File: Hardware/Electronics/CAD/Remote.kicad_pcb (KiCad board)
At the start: 2 copper layers, 191 x 32 mm, 48 parts, among them J1 CONN_01X12, J2 CONN_01X03, J3 CONN_01X05, J4 CONN_01X01, J5 CONN_01X01, J6 CONN_01X24, Q1 AO3418, Q2 Q_NPN_BCE, SW1 SW_DPST_x2, U2 MCP23S17, U3 ESP-12E, U4 LD1117S33CTR

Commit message: update design
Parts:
- removed Q2: Q_NPN_BCE, TO_SOT_Packages_SMD:SOT-23
- removed R14: 10K, Resistors_SMD:R_0805
- removed R15: 1K, Resistors_SMD:R_0805
- removed REF**: ePaper_1.54in, ePaper:ePaper_1.54in
- removed SW1: SW_DPST_x2, Buttons_Switches_SMD:SW_SPST_SKQG
- removed U4: LD1117S33CTR, TO_SOT_Packages_SMD:SOT-223
- added C15: 4,7uF, Capacitors_SMD:C_0805, B.Cu at (167.6, 64.0)
- added C16: 4,7uF, Capacitors_SMD:C_0805, B.Cu at (169.7, 64.0)
- added C17: 4,7uF, Capacitors_SMD:C_0805, B.Cu at (159.5, 68.1)
- added U1: ATMEGA328P-AU, Housings_QFP:TQFP-32_7x7mm_Pitch0.8mm, B.Cu at (159.8, 48.0)
- added Y1: Resonator, Crystals:Resonator_SMD-3pin_7.2x3.0mm, B.Cu at (145.3, 37.3)
- C1: value CP_Small -> 100nF; footprint Capacitor:CP_8x11.5mm_hor -> Capacitors_SMD:C_0805; moved to B.Cu
- C10, C11, C12, C13, C14, C6, C7, C8, C9: value 1uF -> 4,7uF; moved to B.Cu
- C2: value CP_Small -> 1uF; footprint Capacitor:CP_8x11.5mm_hor -> Capacitors_SMD:C_0805; moved to B.Cu
- C3: value 4.7uF -> 1uF; moved to B.Cu
- C4: value 1uF -> 22nF; moved to B.Cu
- C5: value 1uF -> 100nF; moved to B.Cu
- D2: value MBR0520 -> SFH203FA; footprint Diodes_SMD:D_SOD-123 -> LED_castellation:LED_D3.0mm_Horizontal_O6.35mm_Z2.0mm
- D3, D4: value MBR0520 -> MBR0530; moved to B.Cu
- D5: value SFH203FA -> MBR0530; footprint LED_castellation:LED_D3.0mm_Horizontal_O6.35mm_Z2.0mm -> Diodes_SMD:D_SOD-123; moved to B.Cu
- J1: value CONN_01X12 -> CONN_01X01; footprint Terminal:SolderPad_1x12_1.27mm -> SMD_Packages:1Pin
- J2: value CONN_01X03 -> CONN_01X01; footprint Terminal:Pin_Header_SMD_1x3_Angled_2.54mm -> SMD_Packages:1Pin; moved to B.Cu
- J3: value CONN_01X05 -> CONN_02X03; footprint Terminal:SolderPad_1x5_3.81mm -> Pin_Headers:Pin_Header_Straight_2x03_Pitch2.54mm
- J4: value CONN_01X01 -> CONN_01X06; footprint SMD_Packages:1Pin -> Pin_Headers:Pin_Header_Straight_1x06_Pitch2.54mm
- J5: value CONN_01X01 -> CONN_01X12; footprint SMD_Packages:1Pin -> Terminal:SolderPad_1x12_1.27mm
- J6: moved to F.Cu
- L1: footprint Inductors_SMD:L_0805 -> Inductors_SMD:L_1806; moved to B.Cu
- Q1: value AO3418 -> SI1308EDL; footprint TO_SOT_Packages_SMD:SOT-23 -> TO_SOT_Packages_SMD:SOT-323_SC-70; moved to B.Cu
- R1: value 330 -> 10K; moved to B.Cu
- R10, R3: moved to B.Cu
- R11: value 10K -> 1K; moved to B.Cu
- R12: value 10K -> 3; moved to B.Cu
- R13, R4, R5, R7, R8, R9: value 10K -> 4,7K; moved to B.Cu
- R2: value RND 0805 1 10K -> 330; moved to B.Cu
- R6: value 3 -> 4,7K; moved to B.Cu
- U2: value MCP23S17 -> RT9193; footprint Housings_SOIC:SOIC-28W_7.5x17.9mm_Pitch1.27mm -> TO_SOT_Packages_SMD:SOT-23-5; moved to B.Cu
- U3: value ESP-12E -> MCP23S17; footprint ESP8266:ESP-12E_SMD -> SMD_Packages:SOIC-28; moved to B.Cu
- moved C1 95.6 mm to (167.6, 47.5)
- moved D2 76.9 mm to (212.6, 59.7), turned to 90 degrees
- moved R11 76.1 mm to (165.6, 68.1), turned to 270 degrees
- moved R13 67.5 mm to (152.1, 50.8), turned to 0 degrees
- moved D5 61.0 mm to (151.9, 65.5)
- moved R12 54.9 mm to (151.1, 57.9), turned to 0 degrees
- moved R10 54.4 mm to (151.1, 59.9), turned to 180 degrees
- moved R2 53.8 mm to (152.1, 49.0), turned to 180 degrees
- moved R7 48.9 mm to (134.6, 55.4), turned to 270 degrees
- moved R8 42.1 mm to (132.6, 55.4), turned to 270 degrees
- moved J4 38.7 mm to (78.7, 55.6), turned to 90 degrees
- moved R9 37.7 mm to (130.6, 55.4), turned to 270 degrees
- moved R1 36.2 mm to (167.4, 45.7), turned to 0 degrees
- moved R3 27.8 mm to (159.3, 55.4), turned to 90 degrees
- moved C5 27.5 mm to (161.0, 55.4), turned to 270 degrees
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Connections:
- C1 pad 1: Net-(C1-Pad1) -> Earth
- C1 pad 2: GND -> Net-(C1-Pad2)
- C10 pad 1: GND -> Earth
- C10 pad 2: VDD -> +3V3
- C11 pad 1: GND -> Earth
- C11 pad 2: VSH -> Net-(C11-Pad2)
- C12 pad 1: GND -> Earth
- C12 pad 2: VSL -> Net-(C12-Pad2)
- C13 pad 1: GND -> Earth
- C13 pad 2: VCOM -> Net-(C13-Pad2)
- C14 pad 1: GND -> Earth
- C14 pad 2: VPP -> PREVGH
- C2 pad 1: VCI -> Earth
- C2 pad 2: GND -> VCC
- C3 pad 1: GND -> Earth
- C3 pad 2: VCI -> +3V3
- C4 pad 1: Net-(C4-Pad1) -> Earth
- C5 pad 1: PREVGH -> ISP_CS
- C5 pad 2: GND -> UART_DTR
- C6 pad 1: PREVGL -> +3V3
- C6 pad 2: GND -> Earth
- C7 pad 1: GND -> Net-(C7-Pad1)
- C7 pad 2: VGL -> Net-(C7-Pad2)
- C8 pad 1: GND -> Earth
- C8 pad 2: VGH -> Net-(C8-Pad2)
- C9 pad 1: GND -> Earth
- C9 pad 2: VCI -> Net-(C9-Pad2)
- D1 pad 1: GND -> Earth
- D2 pad 1: PREVGH -> IR_LED_IN
- D2 pad 2: Net-(C4-Pad2) -> Net-(D2-Pad2)
- D3 pad 1: Net-(C4-Pad1) -> Earth
- D3 pad 2: PREVGL -> Net-(C7-Pad2)
- D4 pad 1: GND -> Net-(C7-Pad2)
- D4 pad 2: Net-(C4-Pad1) -> PREVGL
- D5 pad 1: Net-(D5-Pad1) -> PREVGH
- D5 pad 2: GND -> Net-(C7-Pad1)
- J1 pad 1: Net-(J1-Pad1) -> VCC
- J2 pad 1: VCI -> Earth
- J3 pad 1: TX -> SPI_MISO
- J3 pad 2: RX -> +3V3
- J3 pad 3: VCI -> SPI_CLK
- J3 pad 4: Net-(J3-Pad4) -> SPI_MOSI
- J3 pad 5: GND -> ISP_CS
- J4 pad 1: Net-(C1-Pad1) -> UART_DTR
- J5 pad 1: GND -> BTN5_IN
- J6 pad 1: Net-(J6-Pad1) -> (no net)
- J6 pad 10: RES# -> RST
- J6 pad 12: CS -> SPI_CS_DISP
- J6 pad 13: CLK -> SPI_CLK
- J6 pad 14: DIN -> SPI_MOSI
- J6 pad 15: VCI -> +3V3
- J6 pad 16: VCI -> +3V3
- J6 pad 17: GND -> Earth
- J6 pad 18: VDD -> Net-(C11-Pad2)
- J6 pad 19: VPP -> Net-(C12-Pad2)
- J6 pad 20: VSH -> Net-(C13-Pad2)
- J6 pad 22: VSL -> Net-(C15-Pad2)
- J6 pad 24: VCOM -> Net-(C17-Pad2)
- J6 pad 4: VGL -> Net-(C8-Pad2)
- J6 pad 5: VGH -> Net-(C9-Pad2)
- J6 pad 6: Net-(J6-Pad6) -> (no net)
- J6 pad 7: Net-(J6-Pad7) -> (no net)
- J6 pad 8: GND -> Net-(J6-Pad8)
- L1 pad 1: Net-(C4-Pad2) -> +3V3
- L1 pad 2: VCI -> Net-(C7-Pad1)
- Q1 pad 3: Net-(C4-Pad2) -> Net-(C7-Pad1)
- R1 pad 1: Net-(R1-Pad1) -> +3V3
- R1 pad 2: Net-(D1-Pad2) -> Net-(D2-Pad2)
- R10 pad 1: GND -> GDR
- R10 pad 2: Net-(J1-Pad8) -> Earth
- R11 pad 1: GND -> Net-(J6-Pad8)
- R11 pad 2: Net-(J1-Pad2) -> Earth
- R12 pad 1: GND -> Earth
- R12 pad 2: Net-(J1-Pad7) -> RESE
- R13 pad 1: VCI -> Earth
- R13 pad 2: Net-(D5-Pad1) -> IR_LED_IN
- R2 pad 1: GND -> IR_LED_OUT
- R2 pad 2: RESET -> Net-(D1-Pad2)
- R3 pad 1: GND -> +3V3
- R3 pad 2: CS -> ISP_CS
- R4 pad 1: VCI -> BTN0_IN
- R4 pad 2: RES# -> Earth
- R5 pad 1: GDR -> BTN1_IN
- R5 pad 2: GND -> Earth
- R6 pad 1: RESE -> BTN2_IN
- R6 pad 2: GND -> Earth
- R7 pad 1: GND -> BTN3_IN
- R7 pad 2: Net-(J1-Pad1) -> Earth
- R8 pad 1: GND -> BTN4_IN
- R8 pad 2: Net-(J1-Pad3) -> Earth
- R9 pad 1: GND -> BTN5_IN
- R9 pad 2: Net-(J1-Pad6) -> Earth
- U2 pad 1: Net-(J1-Pad5) -> VCC
- U2 pad 2: Net-(J1-Pad10) -> Earth
- U2 pad 3: Net-(J1-Pad12) -> VCC
- U2 pad 4: Net-(J1-Pad4) -> Net-(C4-Pad2)
- U2 pad 5: Net-(J1-Pad9) -> +3V3
- U3 pad 1: Net-(U3-Pad1) -> BTN0_IN
- U3 pad 10: CS -> Earth
- U3 pad 11: RES# -> SPI_CS_GPIO_EXP
- U3 pad 12: D/C -> SPI_CLK
- U3 pad 13: BUSY -> SPI_MOSI
- U3 pad 14: RESET -> SPI_MISO
- U3 pad 15: RX -> (no net)
- U3 pad 16: TX -> (no net)
- U3 pad 17: Net-(U2-Pad11) -> (no net)
- U3 pad 18: Net-(U2-Pad14) -> Earth
- U3 pad 19: Net-(U3-Pad19) -> GPIO_EXP_INT
- U3 pad 2: Net-(U3-Pad2) -> BTN1_IN
- U3 pad 20: Net-(U3-Pad20) -> (no net)
- U3 pad 21: Net-(U2-Pad13) -> BTN0_OUT
- U3 pad 22: Net-(U2-Pad12) -> BTN1_OUT
- U3 pad 3: VCI -> BTN2_IN
- U3 pad 4: Net-(Q2-Pad2) -> BTN3_IN
- U3 pad 5: CLK -> BTN4_IN
- U3 pad 6: Net-(R1-Pad1) -> BTN5_IN
- U3 pad 7: DIN -> (no net)
- U3 pad 8: VCI -> (no net)
- U3 pad 9: GND -> +3V3
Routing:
- net Net-(D5-Pad1): track 185.4 -> 0.00 mm, vias 6 -> 0
- net D/C: track 158.7 -> 0.00 mm, vias 4 -> 0
- net GND: track 105.2 -> 0.00 mm, vias 28 -> 0
- net Net-(J1-Pad8): track 104.7 -> 0.00 mm, vias 1 -> 0
- net Net-(J1-Pad6): track 101.9 -> 0.00 mm, vias 1 -> 0
- net TX: track 100.8 -> 0.00 mm, vias 4 -> 0
- net Net-(J1-Pad7): track 99.5 -> 0.00 mm, vias 1 -> 0
- net Net-(D1-Pad2): track 96.9 -> 0.00 mm, vias 2 -> 0
- net RX: track 95.1 -> 0.00 mm, vias 4 -> 0
- net Net-(J1-Pad3): track 93.8 -> 0.00 mm, vias 1 -> 0
- net Net-(J1-Pad1): track 93.5 -> 0.00 mm, vias 1 -> 0
- net Net-(J1-Pad2): track 93.2 -> 0.00 mm, vias 1 -> 0
- net Net-(J1-Pad4): track 89.8 -> 0.00 mm, vias 3 -> 0
- net Net-(C1-Pad1): track 87.6 -> 0.00 mm, vias 5 -> 0
- net Net-(J1-Pad9): track 86.1 -> 0.00 mm, vias 3 -> 0
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- added copper zone on B.Cu, net +3V3
- added copper zone on F.Cu, net Earth
- removed copper zone on B.Cu, net GND
- removed copper zone on F.Cu, net VCI

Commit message: version 1.0 of remote schematics and pcb
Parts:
- removed C2: 1uF, Capacitors_SMD:C_0805
- added Q2: BC817, Package_TO_SOT_SMD:SOT-23, B.Cu at (162.6, 63.2)
- added Q3: BC817, Package_TO_SOT_SMD:SOT-23, B.Cu at (168.1, 63.2)
- added R14: 10K, Resistor_SMD:R_0805_2012Metric, B.Cu at (167.0, 67.2)
- C1, C5: value 100nF -> 0.1uF; footprint Capacitors_SMD:C_0805 -> Capacitor_SMD:C_0805_2012Metric
- C10, C11, C12, C13, C14, C15, C16, C17, C6, C7, C8, C9: footprint Capacitors_SMD:C_0805 -> Capacitor_SMD:C_0805_2012Metric
- C3: value 1uF -> 2,2uF; footprint Capacitors_SMD:C_0805 -> Capacitor_SMD:C_0805_2012Metric
- C4: value 22nF -> 470pF; footprint Capacitors_SMD:C_0805 -> Capacitor_SMD:C_0805_2012Metric
- D1: value IR204A -> WP3A10F3C
- D2: value SFH203FA -> WP3DP3BT
- D3, D4, D5: footprint Diodes_SMD:D_SOD-123 -> Diode_SMD:D_SOD-123
- J3: footprint Pin_Headers:Pin_Header_Straight_2x03_Pitch2.54mm -> Connector_PinHeader_2.54mm:PinHeader_2x03_P2.54mm_Vertical; moved to B.Cu
- J4: footprint Pin_Headers:Pin_Header_Straight_1x06_Pitch2.54mm -> Connector_PinHeader_2.54mm:PinHeader_1x06_P2.54mm_Vertical; moved to B.Cu
- L1: footprint Inductors_SMD:L_1806 -> Inductor_SMD:L_1210_3225Metric
- Q1: footprint TO_SOT_Packages_SMD:SOT-323_SC-70 -> Package_TO_SOT_SMD:SOT-323_SC-70
- R1, R10, R11, R12, R2, R3, R6: footprint Resistors_SMD:R_0805 -> Resistor_SMD:R_0805_2012Metric
- R13, R4, R5, R7, R8, R9: value 4,7K -> 10K; footprint Resistors_SMD:R_0805 -> Resistor_SMD:R_0805_2012Metric
- U1: value ATMEGA328P-AU -> ATmega328P-A; footprint Housings_QFP:TQFP-32_7x7mm_Pitch0.8mm -> Package_QFP:TQFP-32_7x7mm_P0.8mm
- U2: value RT9193 -> MIC5219-3.3YM5; footprint TO_SOT_Packages_SMD:SOT-23-5 -> Package_TO_SOT_SMD:SOT-23-5
- U3: value MCP23S17 -> MCP23S17_SO; footprint SMD_Packages:SOIC-28 -> Package_SO:SOIC-28W_7.5x17.9mm_P1.27mm
- Y1: footprint Crystals:Resonator_SMD-3pin_7.2x3.0mm -> Crystal:Resonator_SMD_Murata_CSTxExxV-3Pin_3.0x1.1mm
- moved C1 30.7 mm to (141.9, 64.1), turned to -90 degrees
- moved Y1 30.1 mm to (156.5, 65.3), turned to 90 degrees
- moved C6 30.1 mm to (133.6, 44.6), turned to -90 degrees
- moved L1 27.8 mm to (136.7, 45.1), turned to -90 degrees
- moved C4 27.2 mm to (120.4, 44.6), turned to 90 degrees
- moved C3 25.3 mm to (127.0, 44.6), turned to 90 degrees
- moved R2 24.9 mm to (169.2, 67.2), turned to -90 degrees
- moved U2 23.8 mm to (123.7, 44.9), turned to 90 degrees
- moved C8 23.5 mm to (169.2, 44.6), turned to -90 degrees
- moved C9 23.5 mm to (167.0, 44.6), turned to -90 degrees
- moved R11 23.5 mm to (164.8, 44.6), turned to 90 degrees
- moved C10 23.5 mm to (162.7, 44.6), turned to -90 degrees
- moved C11 23.5 mm to (160.5, 44.6), turned to -90 degrees
- moved D5 23.4 mm to (140.2, 45.3), turned to -90 degrees
- moved R1 22.2 mm to (161.5, 67.2), turned to 90 degrees
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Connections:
- net D/C renamed D/C
- D1 pad 1: Earth -> Net-(D1-K)
- D1 pad 2: Net-(D1-Pad2) -> Net-(D1-A)
- D2 pad 1: IR_LED_IN -> Net-(D2-K)
- D2 pad 2: Net-(D2-Pad2) -> +3V3
- J4 pad 4: (no net) -> unconnected-(J4-P4-Pad4)
- J6 pad 1: (no net) -> unconnected-(J6-P1-Pad1)
- J6 pad 6: (no net) -> unconnected-(J6-P6-Pad6)
- J6 pad 7: (no net) -> unconnected-(J6-P7-Pad7)
- R1 pad 2: Net-(D2-Pad2) -> IR_LED_IN
- R13 pad 1: Earth -> Net-(D2-K)
- R13 pad 2: IR_LED_IN -> Net-(Q2-B)
- R2 pad 1: IR_LED_OUT -> Net-(D1-A)
- R2 pad 2: Net-(D1-Pad2) -> +3V3
- U1 pad 1: IR_LED_IN -> IR_LED_OUT
- U1 pad 10: (no net) -> unconnected-(U1-PD6-Pad10)
- U1 pad 14: (no net) -> unconnected-(U1-PB2-Pad14)
- U1 pad 19: (no net) -> unconnected-(U1-ADC6-Pad19)
- U1 pad 2: IR_LED_OUT -> IR_LED_IN
- U1 pad 22: (no net) -> unconnected-(U1-ADC7-Pad22)
- U1 pad 25: (no net) -> unconnected-(U1-PC2-Pad25)
- U1 pad 26: (no net) -> unconnected-(U1-PC3-Pad26)
- U1 pad 27: (no net) -> unconnected-(U1-PC4-Pad27)
- U1 pad 28: (no net) -> unconnected-(U1-PC5-Pad28)
- U1 pad 9: (no net) -> unconnected-(U1-PD5-Pad9)
- U3 pad 15: (no net) -> unconnected-(U3-A0-Pad15)
- U3 pad 16: (no net) -> unconnected-(U3-A1-Pad16)
- U3 pad 17: (no net) -> unconnected-(U3-A2-Pad17)
- U3 pad 20: (no net) -> unconnected-(U3-INTA-Pad20)
- U3 pad 27: (no net) -> unconnected-(U3-GPA6-Pad27)
- U3 pad 28: (no net) -> unconnected-(U3-GPA7-Pad28)
- U3 pad 7: (no net) -> unconnected-(U3-GPB6-Pad7)
- U3 pad 8: (no net) -> unconnected-(U3-GPB7-Pad8)
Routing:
- net SPI_CLK: track 0.00 -> 156.7 mm, vias 0 -> 4
- net SPI_MOSI: track 0.00 -> 152.0 mm, vias 0 -> 2
- net BTN5_IN: track 0.00 -> 99.6 mm, vias 0 -> 1
- net SPI_MISO: track 1.84 -> 101.0 mm, vias 0 -> 1
- net BTN4_IN: track 0.00 -> 96.9 mm, vias 0 -> 1
- net BTN3_IN: track 0.00 -> 94.9 mm, vias 0 -> 1
- net ISP_CS: track 0.00 -> 94.2 mm
- net BTN3_OUT: track 0.00 -> 93.9 mm, vias 0 -> 1
- net BTN0_OUT: track 0.00 -> 93.1 mm, vias 0 -> 1
- net VCC: track 0.00 -> 92.6 mm
- net BTN2_IN: track 0.00 -> 90.5 mm, vias 0 -> 1
- net BTN1_IN: track 0.00 -> 88.9 mm, vias 0 -> 1
- net BTN1_OUT: track 0.00 -> 88.2 mm, vias 0 -> 1
- net BTN0_IN: track 0.00 -> 87.3 mm, vias 0 -> 1
- net BTN4_OUT: track 0.00 -> 85.9 mm, vias 0 -> 1
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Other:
- outline, holes or cut-outs redrawn
- net class BatterieFeed removed
- net class Default removed

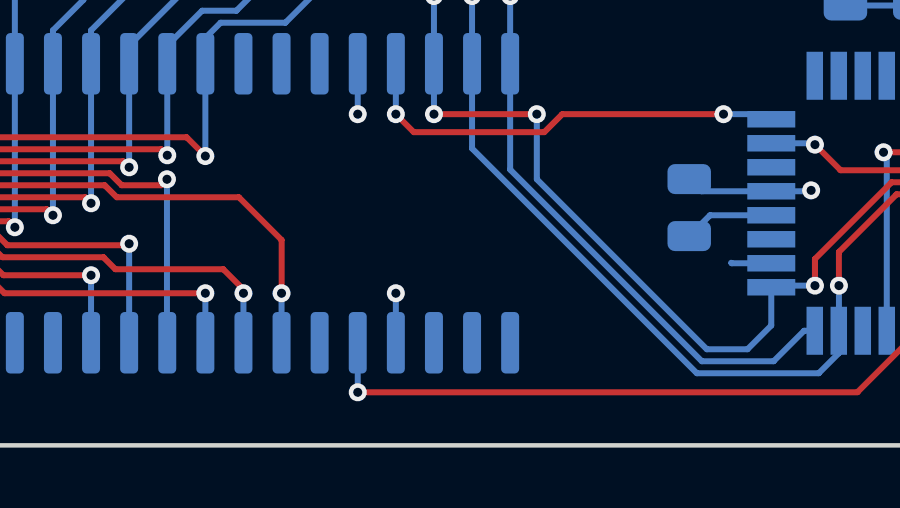
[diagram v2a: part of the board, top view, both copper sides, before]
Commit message: fix expander in schematics and pcb design
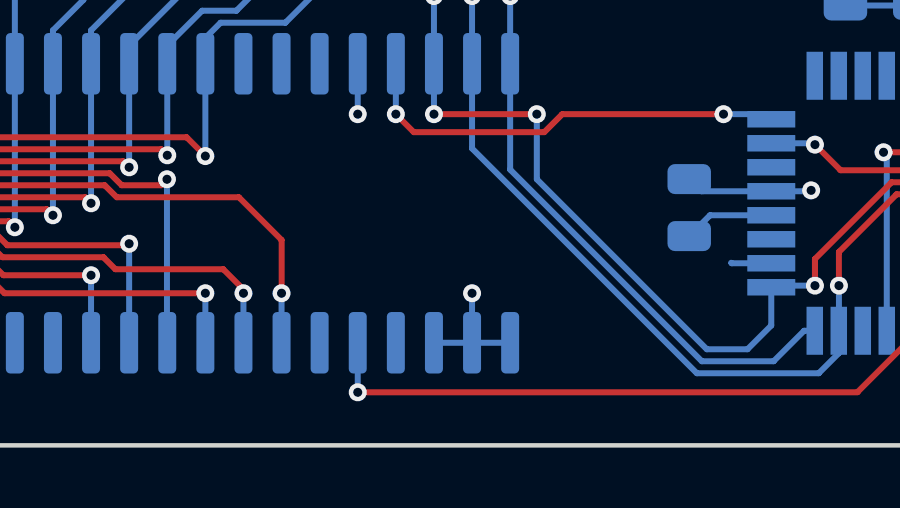
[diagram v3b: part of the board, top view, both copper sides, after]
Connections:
- U3 pad 15: unconnected-(U3-A0-Pad15) -> Earth
- U3 pad 16: unconnected-(U3-A1-Pad16) -> Earth
- U3 pad 17: unconnected-(U3-A2-Pad17) -> Earth
- U3 pad 18: Earth -> +3V3
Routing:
- net Earth: track 77.6 -> 80.1 mm

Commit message: Change IR led resistor from 330 to 33 Ohm
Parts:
- R2: value 330 -> 33
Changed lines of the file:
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@@
     (property "Sheetname" "")
     (attr smd)
-    (fp_text reference "R2" (at 2.7705 -0.127 90) (layer "B.SilkS") hide
+    (fp_text reference "R2" (at 2.7705 -0.127 90) (layer "B.SilkS")
         (effects (font (size 1 1) (thickness 0.15)) (justify mirror))
     )
-    (fp_text value "330" (at 0 -1.65 90) (layer "B.Fab")
+    (fp_text value "33" (at 0 -1.65 90) (layer "B.Fab")
         (effects (font (size 1 1) (thickness 0.15)) (justify mirror))
     )
